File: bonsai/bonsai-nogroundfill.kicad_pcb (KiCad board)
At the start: 2 copper layers, 90.5 x 62.1 mm, 22 parts

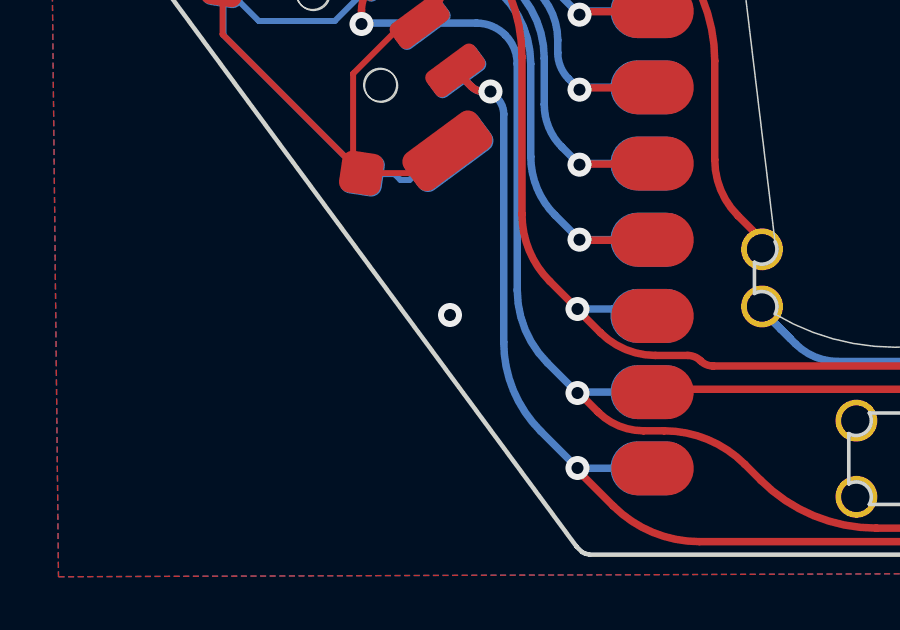
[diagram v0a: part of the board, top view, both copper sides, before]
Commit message: July 15 update
Added gerbers for no ground pour
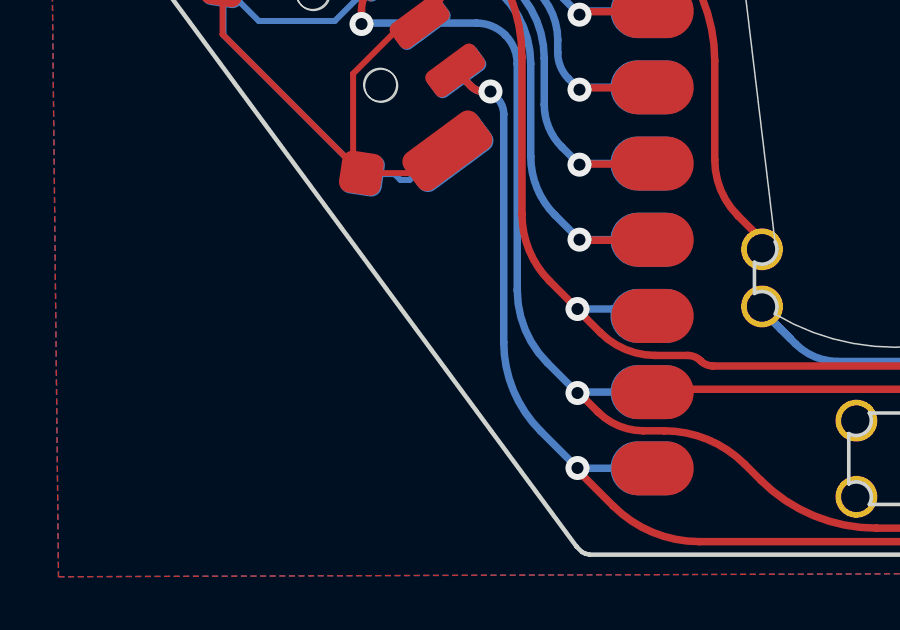
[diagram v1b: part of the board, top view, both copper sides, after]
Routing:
- net GND: vias 4 -> 3
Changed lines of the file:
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@@
-	)
-	(via
-		(at 25.75 67.7)
-		(size 0.8)
-		(drill 0.4)
-		(layers "F.Cu" "B.Cu")
-		(free yes)
-		(net 2)
 	)
 	(via
